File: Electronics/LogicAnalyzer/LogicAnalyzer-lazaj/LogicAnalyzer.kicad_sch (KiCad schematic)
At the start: 54 parts, among them J1 Conn_02x15_Odd_Even, J2 Conn_01x03, J3 Conn_01x03, U1 Pico

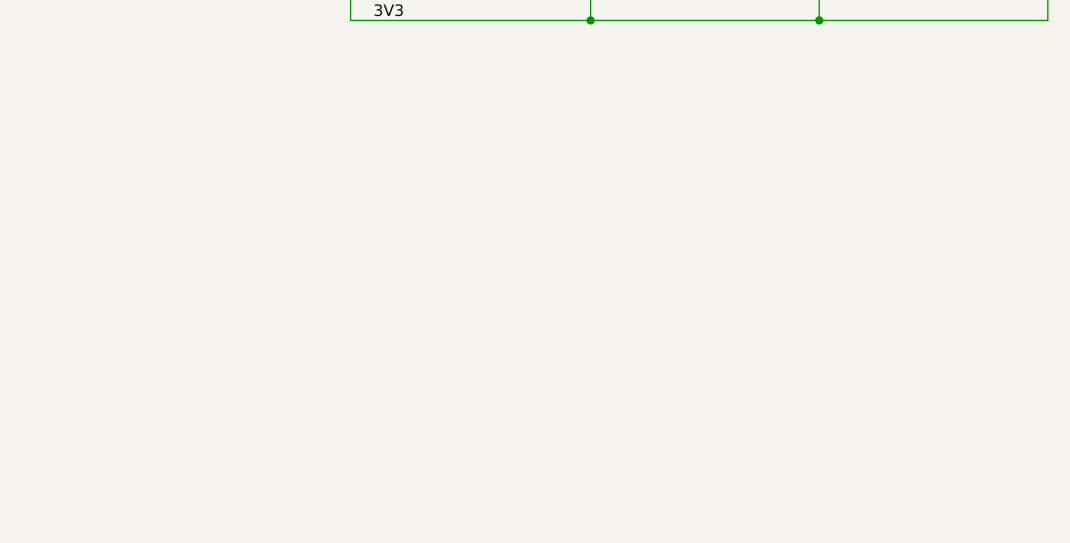
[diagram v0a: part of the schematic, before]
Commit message: sch and pcb: add mountingholes to schematic and pcb to have parity
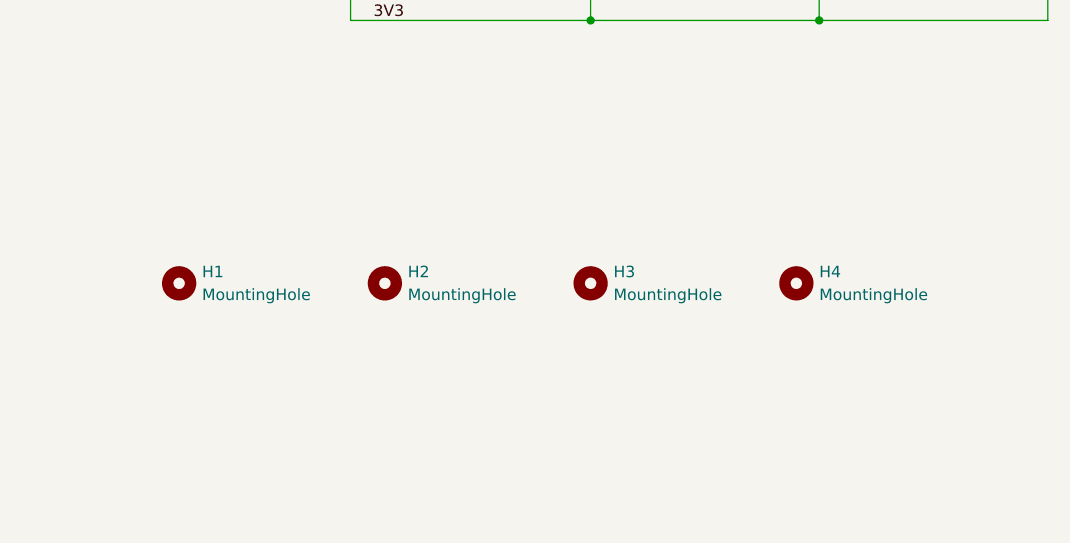
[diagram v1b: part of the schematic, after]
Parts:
- added H1, H2, H3, H4: MountingHole, MountingHole:MountingHole_3.2mm_M3_DIN965_Pad_TopBottom, symbol Mechanical:MountingHole

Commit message: add LCSC partnumbers, turn off refdes for mounting holes
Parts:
- D1: LCSC Part # (none) -> C5345986
- D10, D11, D12, D13, D14, D15, D16, D17, D18, D19, D2, D20, D21, D22, D23, D24, D25, D3, D4, D5, D6, D7, D8, D9: LCSC Part # (none) -> C7420336
- R1: LCSC Part # (none) -> C103211
- R10, R11, R12, R13, R14, R15, R16, R17, R18, R19, R2, R20, R21, R22, R23, R24, R25, R3, R4, R5, R6, R7, R8, R9: LCSC Part # (none) -> C22962

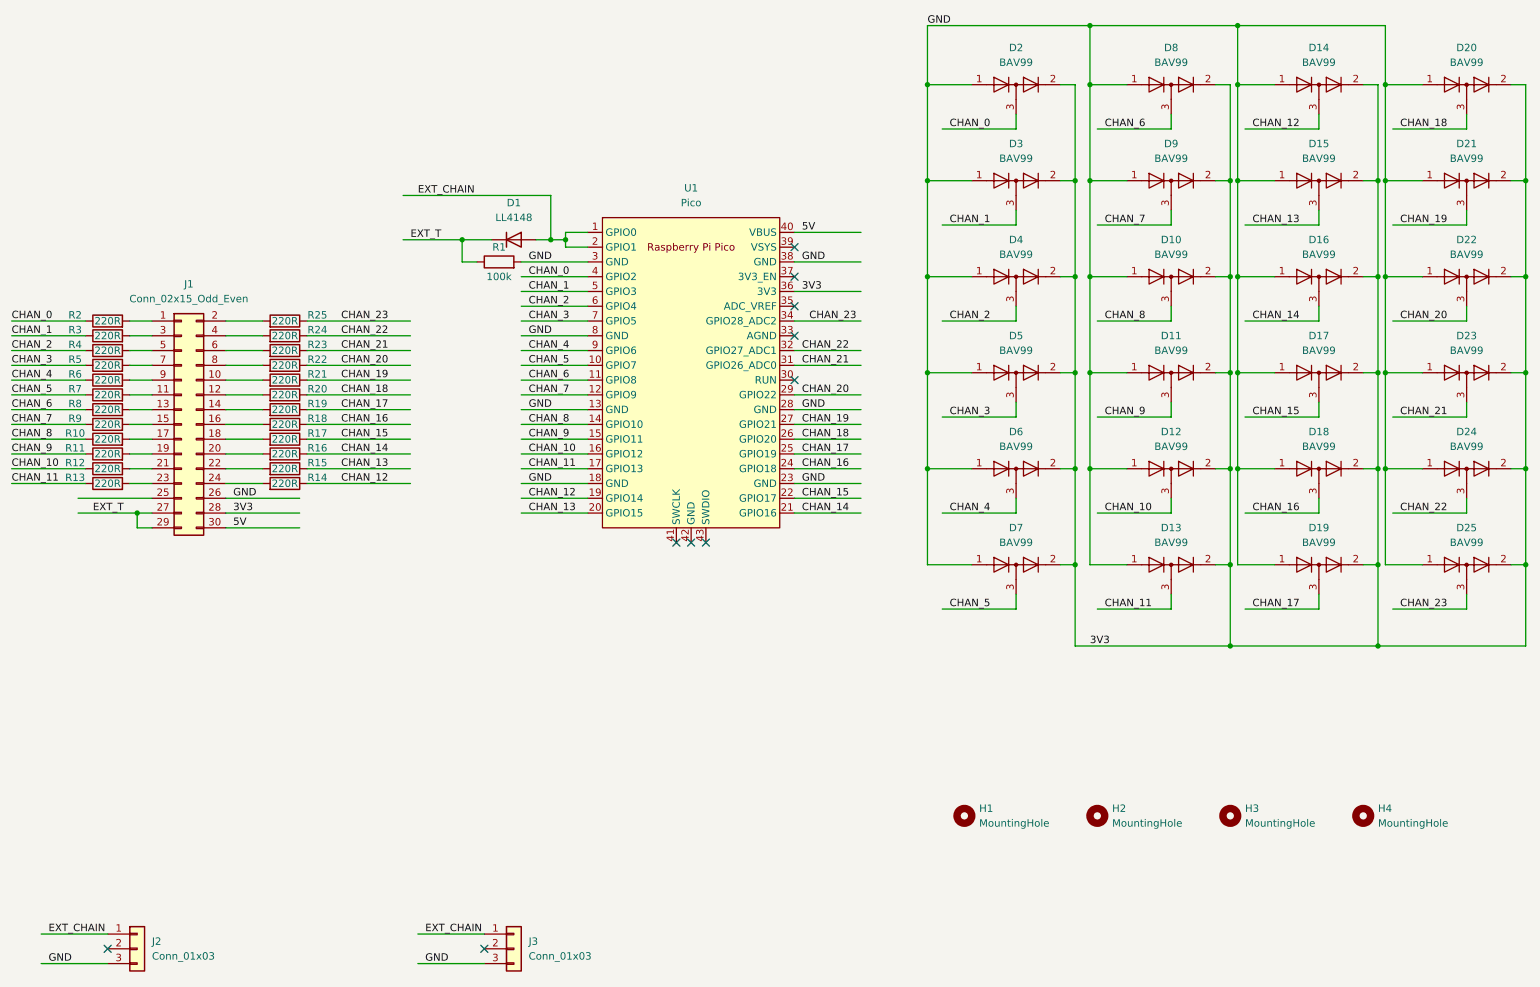
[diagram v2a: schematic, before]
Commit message: mounting holes: change to a footprint that has no electrical connection, pcb: make sure mounting holes are aligned horizontally and vertically
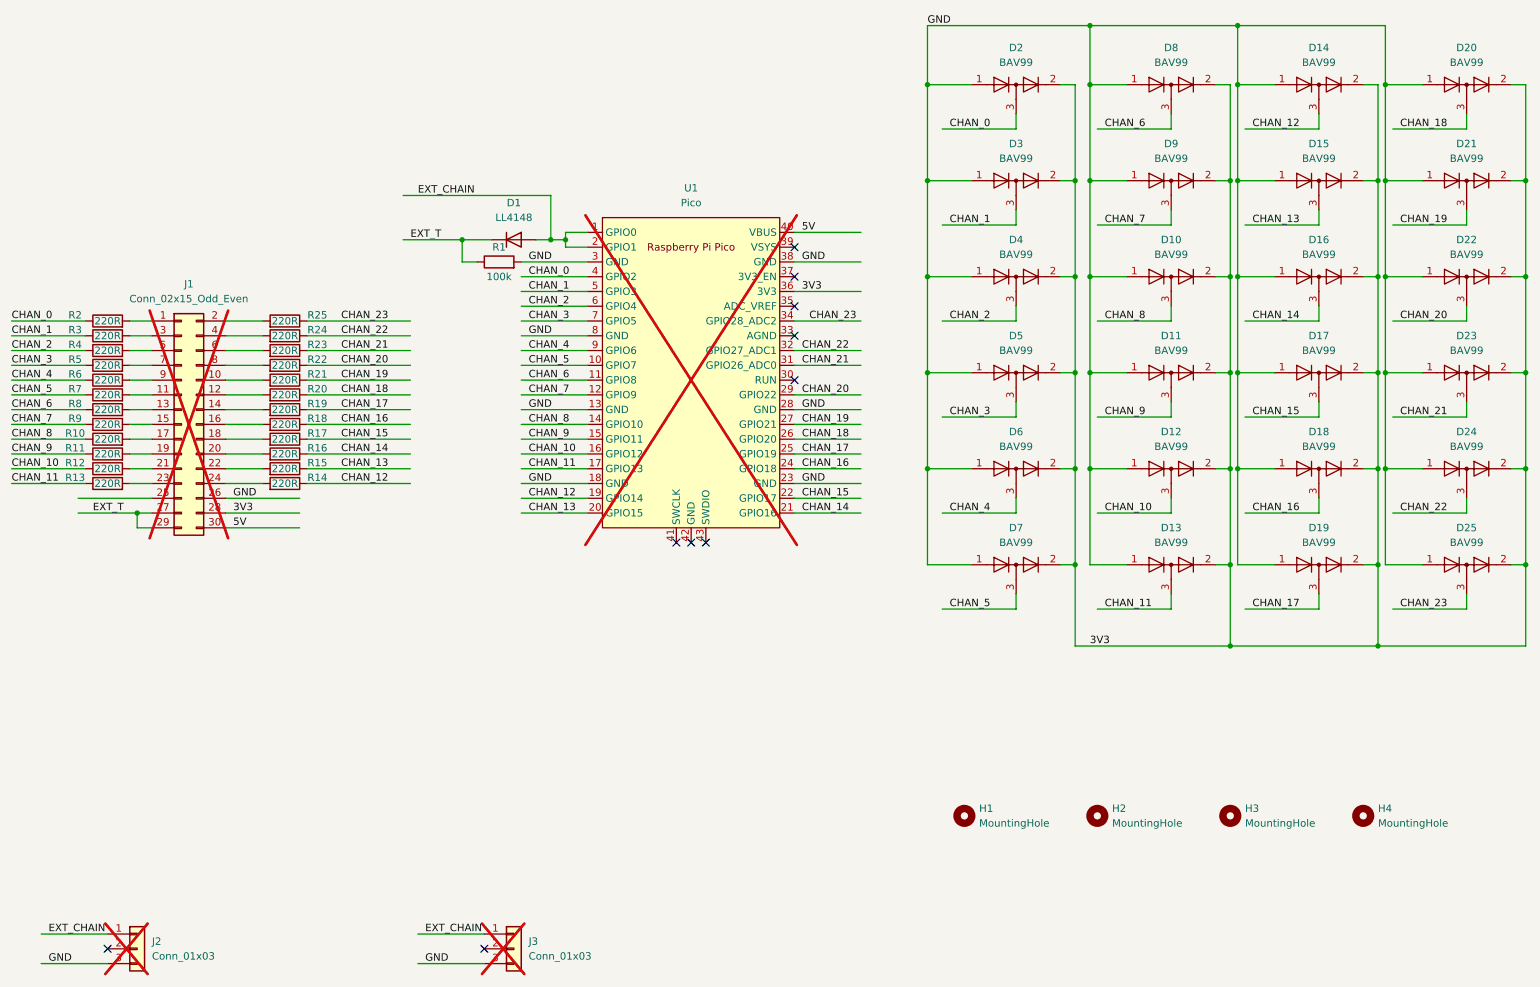
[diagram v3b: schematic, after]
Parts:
- H1, H2, H3, H4: footprint MountingHole:MountingHole_3.2mm_M3_DIN965_Pad_TopBottom -> MountingHole:MountingHole_3.2mm_M3_DIN965
- J1, J2, J3, U1: now not fitted
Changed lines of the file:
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@@
 		(in_bom yes)
 		(on_board yes)
-		(dnp no)
+		(dnp yes)
 		(fields_autoplaced yes)
 		(property "Reference" "U1"
@@
 			)
 		)
-		(property "Footprint" "MountingHole:MountingHole_3.2mm_M3_DIN965_Pad_TopBottom"
+		(property "Footprint" "MountingHole:MountingHole_3.2mm_M3_DIN965"
 			(at 250.19 161.29 0)
 			(effects
@@
 			)
 		)
-		(property "Footprint" "MountingHole:MountingHole_3.2mm_M3_DIN965_Pad_TopBottom"
+		(property "Footprint" "MountingHole:MountingHole_3.2mm_M3_DIN965"
 			(at 181.61 161.29 0)
 			(effects
@@
 			)
 		)
-		(property "Footprint" "MountingHole:MountingHole_3.2mm_M3_DIN965_Pad_TopBottom"
+		(property "Footprint" "MountingHole:MountingHole_3.2mm_M3_DIN965"
 			(at 227.33 161.29 0)
 			(effects
@@
 		(in_bom yes)
 		(on_board yes)
-		(dnp no)
+		(dnp yes)
 		(fields_autoplaced yes)
 		(property "Reference" "J3"
@@
 		(in_bom yes)
 		(on_board yes)
-		(dnp no)
+		(dnp yes)
 		(property "Reference" "J1"
 			(at 48.26 69.85 0)
@@
 			)
 		)
-		(property "Footprint" "MountingHole:MountingHole_3.2mm_M3_DIN965_Pad_TopBottom"
+		(property "Footprint" "MountingHole:MountingHole_3.2mm_M3_DIN965"
 			(at 204.47 161.29 0)
 			(effects
@@
 		(in_bom yes)
 		(on_board yes)
-		(dnp no)
+		(dnp yes)
 		(fields_autoplaced yes)
 		(property "Reference" "J2"
